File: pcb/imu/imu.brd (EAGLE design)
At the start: 16 x 21 mm, 15 parts

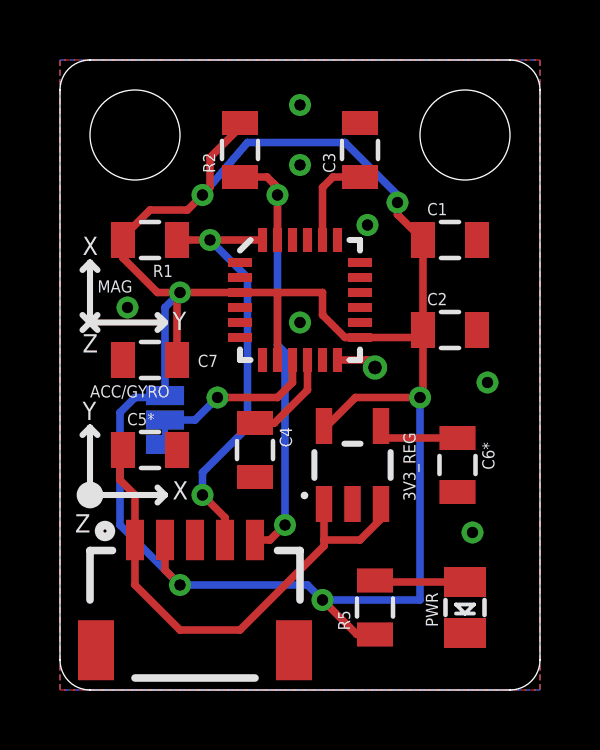
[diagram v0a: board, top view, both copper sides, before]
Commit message: Finalise IMU board schematic/layout. Try to make 3D model (*.emn/emp) files
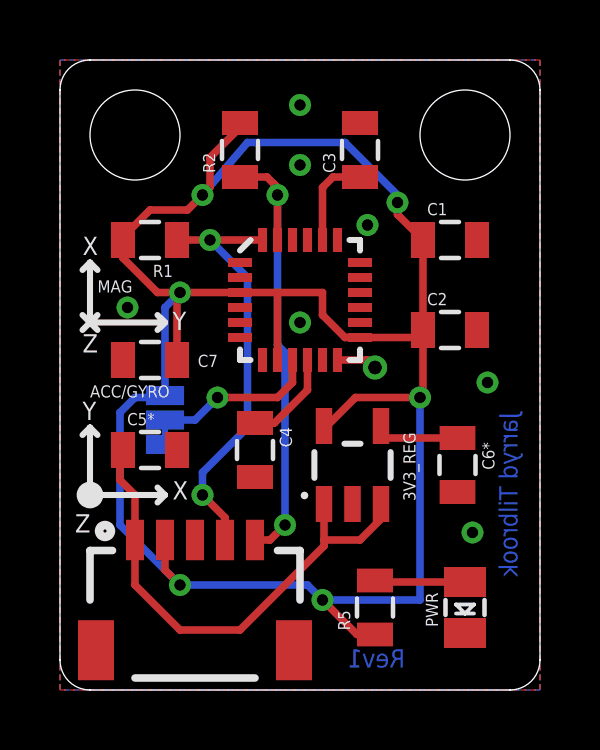
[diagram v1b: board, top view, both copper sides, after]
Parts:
- 3V3_REG: value V_REG_LDOSMD -> (none)
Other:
- board text added: "Rev1"
- board text removed: "rev1"
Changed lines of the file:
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@@
 <setting verticaltext="up"/>
 </settings>
-<grid distance="9.84251969" unitdist="mil" unit="mil" style="lines" multiple="1" display="yes" altdistance="9.84251969" altunitdist="mil" altunit="mil"/>
+<grid distance="0.25" unitdist="mm" unit="mm" style="lines" multiple="1" display="yes" altdistance="0.25" altunitdist="mm" altunit="mm"/>
 <layers>
 <layer number="1" name="Top" color="4" fill="1" visible="yes" active="yes"/>
@@
 <text x="3.75" y="12" size="0.6096" layer="21">Y</text>
 <text x="0.75" y="11.25" size="0.6096" layer="21">Z</text>
-<text x="15.25" y="9.75" size="0.6096" layer="22" ratio="15" rot="SMR270">Jarryd Tilbrook</text>
-<text x="11.5" y="0.75" size="0.6096" layer="22" ratio="12" rot="MR0">rev1</text>
+<text x="15.25" y="9.25" size="0.6096" layer="16" ratio="12" rot="SMR270">Jarryd Tilbrook</text>
+<text x="11.5" y="0.75" size="0.6096" layer="16" ratio="12" rot="MR0">Rev1</text>
+<polygon width="0.1524" layer="42">
+<vertex x="9.25" y="1.5"/>
+<vertex x="11.75" y="1.5"/>
+<vertex x="11.75" y="0.5"/>
+<vertex x="9.25" y="0.5"/>
+</polygon>
+<polygon width="0.1524" layer="42">
+<vertex x="15.5" y="9.5"/>
+<vertex x="14.75" y="9.5"/>
+<vertex x="14.75" y="1.5"/>
+<vertex x="15.5" y="1.5"/>
+</polygon>
 </plain>
 <attributes>
@@
 <attribute name="VALUE" x="12.3" y="3.25" size="0.4064" layer="27" rot="R270"/>
 </element>
-<element name="3V3_REG" library="SparkFun-PowerIC" package="SOT23-5" value="V_REG_LDOSMD" x="9.75" y="7.5" smashed="yes">
+<element name="3V3_REG" library="SparkFun-PowerIC" package="SOT23-5" value="" x="9.75" y="7.5" smashed="yes">
 <attribute name="NAME" x="11.85" y="6.3" size="0.4064" layer="25" rot="R90"/>
 <attribute name="VALUE" x="8.7975" y="7.3095" size="0.4064" layer="27"/>
+<attribute name="PROD_ID" value="VREG-00822" x="9.75" y="7.5" size="1.778" layer="27" display="off"/>
 </element>
 <element name="R5" library="SparkFun-Passives" package="0805" value="150" x="10.5" y="2.75" rot="R90"/>
@@
 <vertex x="16" y="21"/>
 </polygon>
-<contactref element="MPU9150" pad="1"/>
-<contactref element="MPU9150" pad="11"/>
 <via x="13.75" y="5.25" extent="1-16" drill="0.381"/>
 <via x="10.25" y="15.5" extent="1-16" drill="0.381"/>
@@
 <via x="8" y="17.5" extent="1-16" drill="0.381"/>
 <via x="8" y="19.5" extent="1-16" drill="0.381"/>
+<contactref element="MPU9150" pad="1"/>
+<contactref element="MPU9150" pad="11"/>
+<wire x1="8" y1="12.25" x2="8.75" y2="11" width="0" layer="19" extent="1-1"/>
 </signal>
 <signal name="VCC">

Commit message: Revise IMU board - add date and board title
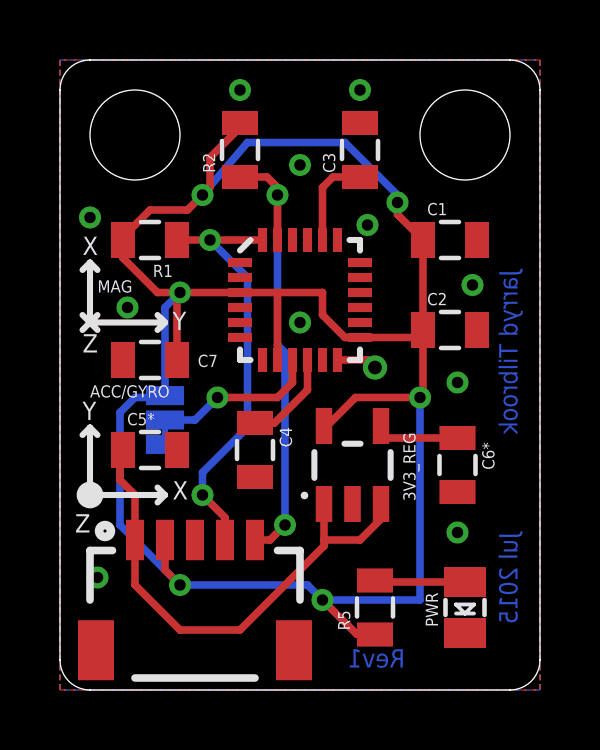
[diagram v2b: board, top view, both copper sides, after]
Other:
- board text added: "Jul 2015"
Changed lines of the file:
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@@
 <text x="3.75" y="12" size="0.6096" layer="21">Y</text>
 <text x="0.75" y="11.25" size="0.6096" layer="21">Z</text>
-<text x="15.25" y="9.25" size="0.6096" layer="16" ratio="12" rot="SMR270">Jarryd Tilbrook</text>
+<text x="15.25" y="14" size="0.6096" layer="16" ratio="12" rot="SMR270">Jarryd Tilbrook</text>
 <text x="11.5" y="0.75" size="0.6096" layer="16" ratio="12" rot="MR0">Rev1</text>
-<polygon width="0.1524" layer="42">
-<vertex x="9.25" y="1.5"/>
-<vertex x="11.75" y="1.5"/>
-<vertex x="11.75" y="0.5"/>
-<vertex x="9.25" y="0.5"/>
-</polygon>
-<polygon width="0.1524" layer="42">
-<vertex x="15.5" y="9.5"/>
-<vertex x="14.75" y="9.5"/>
-<vertex x="14.75" y="1.5"/>
-<vertex x="15.5" y="1.5"/>
-</polygon>
+<text x="15.25" y="5.25" size="0.6096" layer="16" ratio="12" rot="SMR270">Jul 2015</text>
+<rectangle x1="14.5" y1="0.75" x2="15.5" y2="5.5" layer="42"/>
+<rectangle x1="9.25" y1="0.5" x2="11.75" y2="1.5" layer="42"/>
+<rectangle x1="14.5" y1="6.25" x2="15.5" y2="14.25" layer="42"/>
 </plain>
 <attributes>
@@
 <vertex x="16" y="21"/>
 </polygon>
-<via x="13.75" y="5.25" extent="1-16" drill="0.381"/>
+<via x="13.25" y="5.25" extent="1-16" drill="0.381"/>
 <via x="10.25" y="15.5" extent="1-16" drill="0.381"/>
-<via x="14.25" y="10.25" extent="1-16" drill="0.381"/>
+<via x="13.25" y="10.25" extent="1-16" drill="0.381"/>
 <via x="2.25" y="12.75" extent="1-16" drill="0.381"/>
 <via x="8" y="12.25" extent="1-16" drill="0.381"/>
 <via x="8" y="17.5" extent="1-16" drill="0.381"/>
-<via x="8" y="19.5" extent="1-16" drill="0.381"/>
+<via x="6" y="20" extent="1-16" drill="0.381"/>
 <contactref element="MPU9150" pad="1"/>
 <contactref element="MPU9150" pad="11"/>
-<wire x1="8" y1="12.25" x2="8.75" y2="11" width="0" layer="19" extent="1-1"/>
+<via x="13.75" y="13.5" extent="1-16" drill="0.381"/>
+<via x="10" y="20" extent="1-16" drill="0.381"/>
+<via x="1.25" y="3.75" extent="1-16" drill="0.381"/>
+<via x="1" y="15.75" extent="1-16" drill="0.381"/>
 </signal>
 <signal name="VCC">

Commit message: Finalise rev2 board, add IMU parts list
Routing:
- net VCC: track 72.9 -> 71.0 mm
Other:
- board text added: "MPU-9150 Breakout"
- board text added: "Rev2"
- board text removed: "Rev1"
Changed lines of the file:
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@@
 <hole x="13.5" y="18.5" drill="3"/>
 <hole x="2.5" y="18.5" drill="3"/>
-<text x="3" y="2.7432" size="0.8128" layer="22" rot="MR270">VIN</text>
-<text x="4" y="3" size="0.8128" layer="22" rot="MR270">VCC</text>
-<text x="5" y="3" size="0.8128" layer="22" rot="MR270">GND</text>
-<text x="7" y="3" size="0.8128" layer="22" rot="MR270">SCL</text>
-<text x="6" y="3" size="0.8128" layer="22" rot="MR270">SDA</text>
+<text x="3" y="2.7432" size="0.8128" layer="22" ratio="11" rot="MR270">VIN</text>
+<text x="4" y="3" size="0.8128" layer="22" ratio="11" rot="MR270">VCC</text>
+<text x="5" y="3" size="0.8128" layer="22" ratio="11" rot="MR270">GND</text>
+<text x="7" y="3" size="0.8128" layer="22" ratio="11" rot="MR270">SCL</text>
+<text x="6" y="3" size="0.8128" layer="22" ratio="11" rot="MR270">SDA</text>
 <text x="3" y="7.25" size="0.4064" layer="22" rot="MR180">GND</text>
 <text x="3" y="11.25" size="0.4064" layer="22" rot="MR180">VCC</text>
 <text x="1.2" y="8" size="0.4064" layer="22" rot="MR90">SELECT</text>
-<text x="10.5" y="11.5" size="0.4064" layer="22" rot="MR0" align="bottom-center">INT</text>
+<text x="10.5" y="9.75" size="0.4064" layer="22" ratio="11" rot="MR0" align="bottom-center">INT</text>
 <wire x1="1" y1="6.5" x2="3.5" y2="6.5" width="0.2032" layer="21"/>
 <wire x1="3.25" y1="6.75" x2="3.5" y2="6.5" width="0.2032" layer="21"/>
@@
 <wire x1="1.25" y1="8.5" x2="1" y2="8.75" width="0.2032" layer="21"/>
 <circle x="1" y="6.5" radius="0.254" width="0.381" layer="21"/>
-<text x="3.75" y="6.35" size="0.6096" layer="21">X</text>
-<text x="0.75" y="9" size="0.6096" layer="21">Y</text>
-<text x="0.5" y="5.25" size="0.6096" layer="21">Z</text>
-<text x="1" y="9.75" size="0.4064" layer="21">ACC/GYRO</text>
-<text x="1.25" y="13.25" size="0.4064" layer="21">MAG</text>
+<text x="3.75" y="6.35" size="0.6096" layer="21" ratio="11">X</text>
+<text x="0.75" y="9" size="0.6096" layer="21" ratio="11">Y</text>
+<text x="0.5" y="5.25" size="0.6096" layer="21" ratio="11">Z</text>
+<text x="1" y="9.75" size="0.4064" layer="21" ratio="11">ACC/GYRO</text>
+<text x="1.25" y="13.25" size="0.4064" layer="21" ratio="11">MAG</text>
 <wire x1="1" y1="12.25" x2="3.5" y2="12.25" width="0.2032" layer="21"/>
 <wire x1="3.25" y1="12.5" x2="3.5" y2="12.25" width="0.2032" layer="21"/>
@@
 <wire x1="0.75" y1="12" x2="1.25" y2="12.5" width="0.2032" layer="21"/>
 <wire x1="0.75" y1="12.5" x2="1.25" y2="12" width="0.2032" layer="21"/>
-<text x="0.75" y="14.5" size="0.6096" layer="21">X</text>
-<text x="3.75" y="12" size="0.6096" layer="21">Y</text>
-<text x="0.75" y="11.25" size="0.6096" layer="21">Z</text>
+<text x="0.75" y="14.5" size="0.6096" layer="21" ratio="11">X</text>
+<text x="3.75" y="12" size="0.6096" layer="21" ratio="11">Y</text>
+<text x="0.75" y="11.25" size="0.6096" layer="21" ratio="11">Z</text>
 <text x="15.25" y="14" size="0.6096" layer="16" ratio="12" rot="SMR270">Jarryd Tilbrook</text>
-<text x="11.5" y="0.75" size="0.6096" layer="16" ratio="12" rot="MR0">Rev1</text>
+<text x="11.5" y="0.75" size="0.6096" layer="16" ratio="12" rot="MR0">Rev2</text>
 <text x="15.25" y="5.25" size="0.6096" layer="16" ratio="12" rot="SMR270">Jul 2015</text>
 <rectangle x1="14.5" y1="0.75" x2="15.5" y2="5.5" layer="42"/>
 <rectangle x1="9.25" y1="0.5" x2="11.75" y2="1.5" layer="42"/>
 <rectangle x1="14.5" y1="6.25" x2="15.5" y2="14.25" layer="42"/>
+<text x="8" y="11.25" size="1.016" layer="22" ratio="11" rot="MR0" align="bottom-center">MPU-9150
+Breakout</text>
 </plain>
 <attributes>
@@
 <wire x1="12.1" y1="9.85" x2="12.1" y2="12" width="0.254" layer="1"/>
 <via x="12" y="9.75" extent="1-16" drill="0.381"/>
-<wire x1="12" y1="9.75" x2="12" y2="3" width="0.254" layer="16"/>
-<wire x1="12" y1="3" x2="8.75" y2="3" width="0.254" layer="16"/>
 <wire x1="3.25" y1="13.25" x2="2.1" y2="14.4" width="0.254" layer="1"/>
 <wire x1="2.1" y1="14.4" x2="2.1" y2="15" width="0.254" layer="1"/>
@@
 <wire x1="4.75" y1="16.5" x2="5" y2="16.75" width="0.254" layer="1"/>
 <wire x1="5" y1="16.75" x2="5" y2="17.75" width="0.254" layer="1"/>
+<wire x1="8.75" y1="3" x2="12" y2="6.25" width="0.254" layer="16"/>
+<wire x1="12" y1="6.25" x2="12" y2="9.75" width="0.254" layer="16"/>
 </signal>
 <signal name="SDA">
@@
 </board>
 </drawing>
+<compatibility>
+<note version="6.3" minversion="6.2.2" severity="warning">
+Since Version 6.2.2 text objects can contain more than one line,
+which will not be processed correctly with this version.
+</note>
+</compatibility>
 </eagle>
